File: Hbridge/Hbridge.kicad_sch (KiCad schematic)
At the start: 11 parts, among them Q401 P-channel, Q402 N-channel, Q403 P-channel, Q404 N-channel, Q501 BC847, Q506 BC847

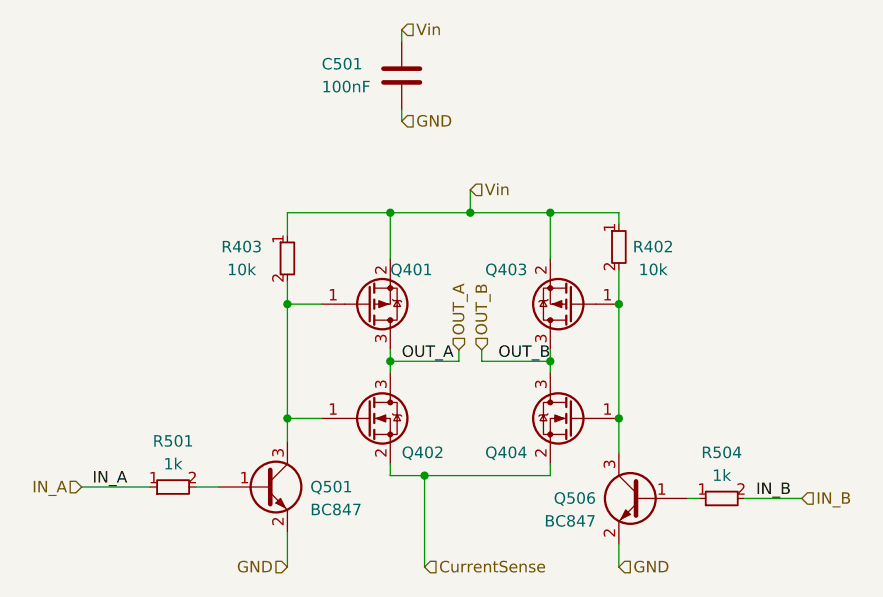
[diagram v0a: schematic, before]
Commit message: removed hierarchial labels for power symbols and replaced them with actual power symbols also updated footprint of the inductor of the 5V buck
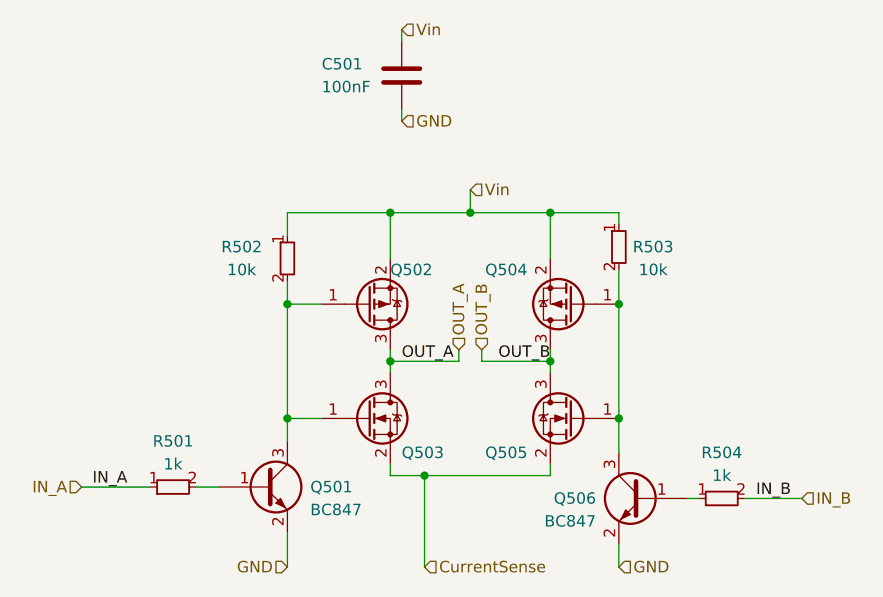
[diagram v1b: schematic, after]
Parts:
- renumbered Q401 to Q502, Q402 to Q503, Q403 to Q504, Q404 to Q505, R403 to R502, R402 to R503
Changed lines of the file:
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@@
   (symbol (lib_id "Transistor_FET:AO3400A") (at 172.72 74.93 0) (mirror y) (unit 1)
     (in_bom yes) (on_board yes) (dnp no)
-    (property "Reference" "Q404" (at 167.64 78.74 0)
+    (property "Reference" "Q505" (at 167.64 78.74 0)
       (effects (font (size 1.27 1.27)) (justify left))
     )
@@
   (symbol (lib_id "resistors_0603:R_10k_0603") (at 140.97 57.15 0) (unit 1)
     (in_bom yes) (on_board yes) (dnp no)
-    (property "Reference" "R403" (at 135.89 55.88 0)
+    (property "Reference" "R502" (at 135.89 55.88 0)
       (effects (font (size 1.27 1.27)))
     )
@@
   (symbol (lib_id "Transistor_FET:AO3400A") (at 149.86 74.93 0) (unit 1)
     (in_bom yes) (on_board yes) (dnp no)
-    (property "Reference" "Q402" (at 153.67 78.74 0)
+    (property "Reference" "Q503" (at 153.67 78.74 0)
       (effects (font (size 1.27 1.27)) (justify left))
     )
@@
   (symbol (lib_id "resistors_0603:R_10k_0603") (at 177.8 55.88 0) (unit 1)
     (in_bom yes) (on_board yes) (dnp no)
-    (property "Reference" "R402" (at 181.61 55.88 0)
+    (property "Reference" "R503" (at 181.61 55.88 0)
       (effects (font (size 1.27 1.27)))
     )
@@
   (symbol (lib_id "Transistor_FET:AO3401A") (at 149.86 62.23 0) (mirror x) (unit 1)
     (in_bom yes) (on_board yes) (dnp no)
-    (property "Reference" "Q401" (at 152.4 58.42 0)
+    (property "Reference" "Q502" (at 152.4 58.42 0)
       (effects (font (size 1.27 1.27)) (justify left))
     )
@@
   (symbol (lib_id "Transistor_FET:AO3401A") (at 172.72 62.23 180) (unit 1)
     (in_bom yes) (on_board yes) (dnp no)
-    (property "Reference" "Q403" (at 167.64 58.42 0)
-      (effects (font (size 1.27 1.27)) (justify left))
-    )
+    (property "Reference" "Q504" (at 167.64 58.42 0)
+      (effects (font (size 1.27 1.27)) (justify left))
+    )
